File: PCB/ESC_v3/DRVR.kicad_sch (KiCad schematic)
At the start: 14 parts, among them U2 DRV8323SRTAT

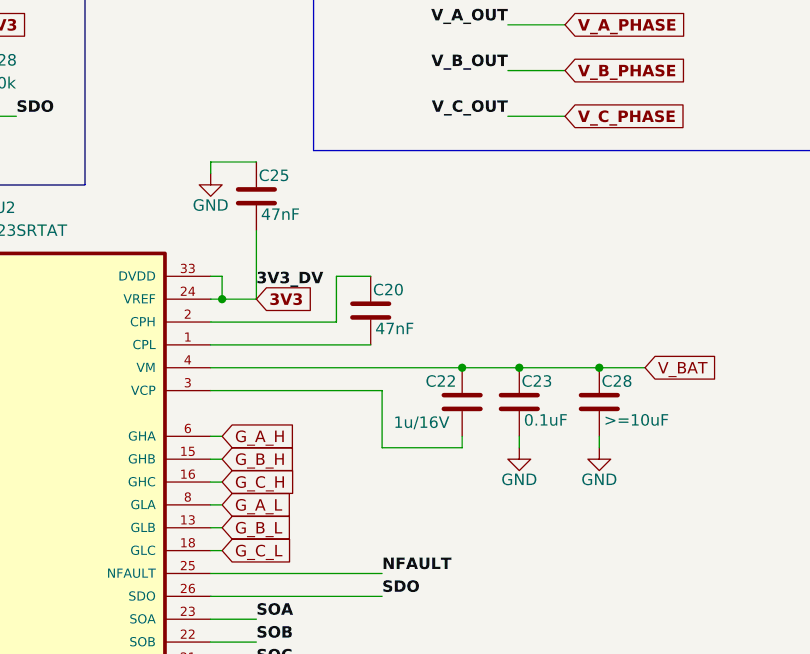
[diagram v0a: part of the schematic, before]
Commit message: Fix DRVR schematic wiring and PCB nets
Clean up DRVR.kicad_sch by adding/removing junctions and wires, rerouting traces and repositioning symbols; update component properties (capacitor values/ratings and label positions). Update ESC_v3.kicad_pcb to match schematic changes: reorder/renumber nets, correct pin/net assignments and adjust footprints/placements. Remove many outdated ESC_v3-backups ZIPs and add new timestamped backup ZIPs; add STM/STM.ioc and update MCU.kicad_sch and related project files. These changes correct net mappings and tidy schematic/PCB routing and metadata.
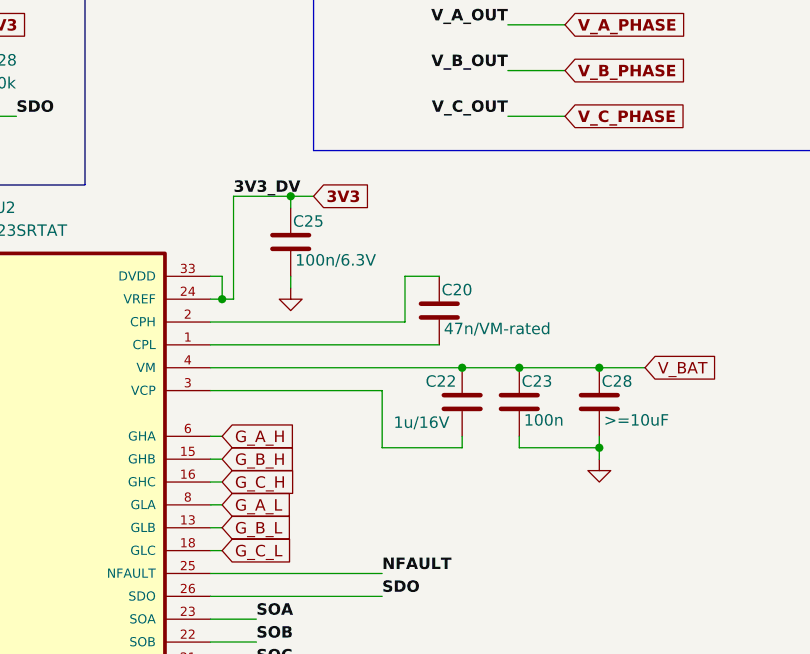
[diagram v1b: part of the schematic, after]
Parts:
- C20: value 47nF -> 47n/VM-rated
- C23: value 0.1uF -> 100n
- C25: value 47nF -> 100n/6.3V
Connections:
- net 3V3: now also C25.1; no longer C25.2
- net GND: now also C25.2; no longer C25.1
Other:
- moved on the sheet: C20, C25

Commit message: Updates
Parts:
- added C34: 100n/6.3V, Capacitor_SMD:C_0805_2012Metric, symbol Device:C
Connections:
- net EN_DV: now also C34.1
- net GND: now also C34.2
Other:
- moved on the sheet: R26
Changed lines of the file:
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@@
 	)
 	(junction
-		(at 40.64 41.91)
+		(at 41.91 35.56)
 		(diameter 0)
 		(color 0 0 0 0)
@@
 	(wire
 		(pts
-			(xy 40.64 41.91) (xy 45.72 41.91)
+			(xy 41.91 35.56) (xy 46.99 35.56)
 		)
 		(stroke
@@
 	(wire
 		(pts
-			(xy 40.64 41.91) (xy 40.64 40.64)
+			(xy 41.91 35.56) (xy 41.91 34.29)
 		)
 		(stroke
@@
 	(wire
 		(pts
+			(xy 41.91 35.56) (xy 41.91 36.83)
+		)
+		(stroke
+			(width 0)
+			(type default)
+		)
+	)
+	(wire
+		(pts
 			(xy 100.33 115.57) (xy 104.14 115.57)
 		)
@@
 	(wire
 		(pts
-			(xy 40.64 31.75) (xy 40.64 33.02)
+			(xy 41.91 25.4) (xy 41.91 26.67)
 		)
 		(stroke
@@
 	(wire
 		(pts
-			(xy 35.56 41.91) (xy 40.64 41.91)
+			(xy 36.83 35.56) (xy 41.91 35.56)
 		)
 		(stroke
@@
 	(wire
 		(pts
+			(xy 41.91 44.45) (xy 41.91 45.72)
+		)
+		(stroke
+			(width 0)
+			(type default)
+		)
+	)
+	(wire
+		(pts
 			(xy 30.48 69.85) (xy 30.48 73.66)
 		)
@@
 	)
 	(label "EN_DV"
-		(at 35.56 41.91 180)
+		(at 36.83 35.56 180)
 		(effects
 			(font
@@
 	)
 	(label "ENABLE"
-		(at 45.72 41.91 0)
+		(at 46.99 35.56 0)
 		(effects
 			(font
@@
 	(global_label "3V3"
 		(shape input)
-		(at 40.64 31.75 180)
+		(at 41.91 25.4 180)
 		(fields_autoplaced yes)
 		(effects
@@
 		)
 		(property "Intersheetrefs" "${INTERSHEET_REFS}"
-			(at 33.6712 31.75 0)
+			(at 34.9412 25.4 0)
 			(effects
 				(font
@@
 	(symbol
 		(lib_id "Device:C")
+		(at 41.91 40.64 0)
+		(unit 1)
+		(exclude_from_sim no)
+		(in_bom yes)
+		(on_board yes)
+		(dnp no)
+		(property "Reference" "C34"
+			(at 42.164 38.354 0)
+			(effects
+				(font
+					(size 1.27 1.27)
+				)
+				(justify left)
+			)
+		)
+		(property "Value" "100n/6.3V"
+			(at 42.418 42.672 0)
+			(effects
+				(font
+					(size 1.27 1.27)
+				)
+				(justify left)
+			)
+		)
+		(property "Footprint" "Capacitor_SMD:C_0805_2012Metric"
+			(at 42.8752 44.45 0)
+			(effects
+				(font
+					(size 1.27 1.27)
+				)
+				(hide yes)
+			)
+		)
+		(property "Datasheet" "~"
+			(at 41.91 40.64 0)
+			(effects
+				(font
+					(size 1.27 1.27)
+				)
+				(hide yes)
+			)
+		)
+		(property "Description" "Unpolarized capacitor"
+			(at 41.91 40.64 0)
+			(effects
+				(font
+					(size 1.27 1.27)
+				)
+				(hide yes)
+			)
+		)
+		(pin "1"
+		)
+		(pin "2"
+		)
+		(instances
+			(project "ESC_v3"
+				(path "/bb7f65bd-c3d2-4eba-8e72-fdc4c3d3399c/c36682af-7334-4ae4-b708-5014138612ef"
+					(reference "C34")
+					(unit 1)
+				)
+			)
+		)
+	)
+	(symbol
+		(lib_id "Device:C")
 		(at 184.15 73.66 0)
 		(unit 1)
@@
 	)
 	(symbol
+		(lib_id "power:GND")
+		(at 41.91 45.72 0)
+		(unit 1)
+		(exclude_from_sim no)
+		(in_bom yes)
+		(on_board yes)
+		(dnp no)
+		(property "Reference" "#PWR020"
+			(at 41.91 52.07 0)
+			(effects
+				(font
+					(size 1.27 1.27)
+				)
+				(hide yes)
+			)
+		)
+		(property "Value" "GND"
+			(at 41.91 49.276 0)
+			(effects
+				(font
+					(size 1.27 1.27)
+				)
+				(hide yes)
+			)
+		)
+		(property "Footprint" ""
+			(at 41.91 45.72 0)
+			(effects
+				(font
+					(size 1.27 1.27)
+				)
+				(hide yes)
+			)
+		)
+		(property "Datasheet" ""
+			(at 41.91 45.72 0)
+			(effects
+				(font
+					(size 1.27 1.27)
+				)
+				(hide yes)
+			)
+		)
+		(property "Description" "Power symbol creates a global label with name \"GND\" , ground"
+			(at 41.91 45.72 0)
+			(effects
+				(font
+					(size 1.27 1.27)
+				)
+				(hide yes)
+			)
+		)
+		(pin "1"
+		)
+		(instances
+			(project "ESC_v3"
+				(path "/bb7f65bd-c3d2-4eba-8e72-fdc4c3d3399c/c36682af-7334-4ae4-b708-5014138612ef"
+					(reference "#PWR020")
+					(unit 1)
+				)
+			)
+		)
+	)
+	(symbol
 		(lib_id "Device:R")
-		(at 40.64 36.83 180)
+		(at 41.91 30.48 180)
 		(unit 1)
 		(exclude_from_sim no)
@@
 		(dnp no)
 		(property "Reference" "R26"
-			(at 44.069 35.687 0)
+			(at 45.339 29.337 0)
 			(effects
 				(font
@@
 		)
 		(property "Value" "10k"
-			(at 44.069 38.227 0)
+			(at 45.339 31.877 0)
 			(effects
 				(font
@@
 		)
 		(property "Footprint" "Resistor_SMD:R_0603_1608Metric"
-			(at 42.418 36.83 90)
+			(at 43.688 30.48 90)
 			(effects
 				(font
@@
 		)
 		(property "Datasheet" "~"
-			(at 40.64 36.83 0)
+			(at 41.91 30.48 0)
 			(effects
 				(font
@@
 		)
 		(property "Description" "Resistor"
-			(at 40.64 36.83 0)
+			(at 41.91 30.48 0)
 			(effects
 				(font
@@
 					(size 1.27 1.27)
 				)
+				(hide yes)
 			)
 		)

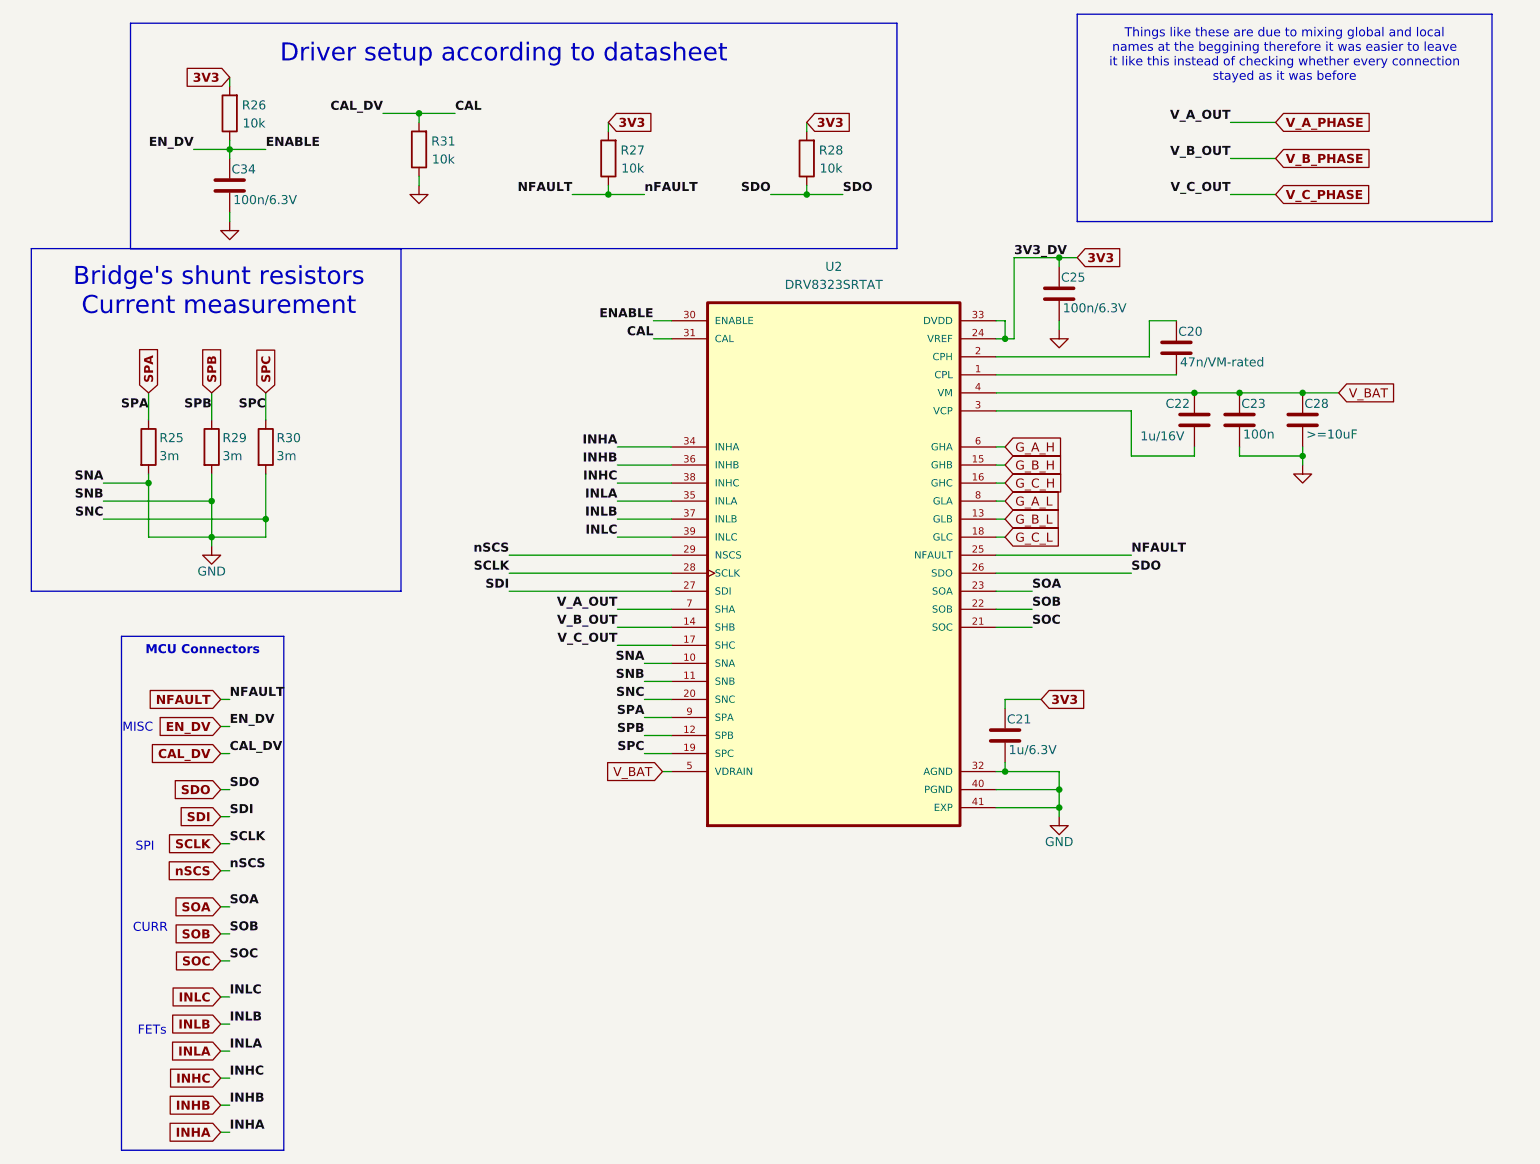
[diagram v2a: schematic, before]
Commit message: Update PCB layout and driver schematic
Adjust KiCad project files: many PCB footprint positions/rotations/uuids and silk/pad orientations updated, trace segments and widths adjusted, vias added/moved (several tented/free vias), and zone_connect enabled on referenced footprints. Correct MCU pin net assignments (PB4/PB5/PB6 / NFAULT / EN_DV) and other net fixes. In DRVR schematic change stroke styles to dashed and update a capacitor value from ">=10uF" to "22u". Remove several old backup zip files and add new backup snapshots. Miscellaneous small .kicad_prl/.kicad_sch/.ioc updates included for consistency and routing cleanup.
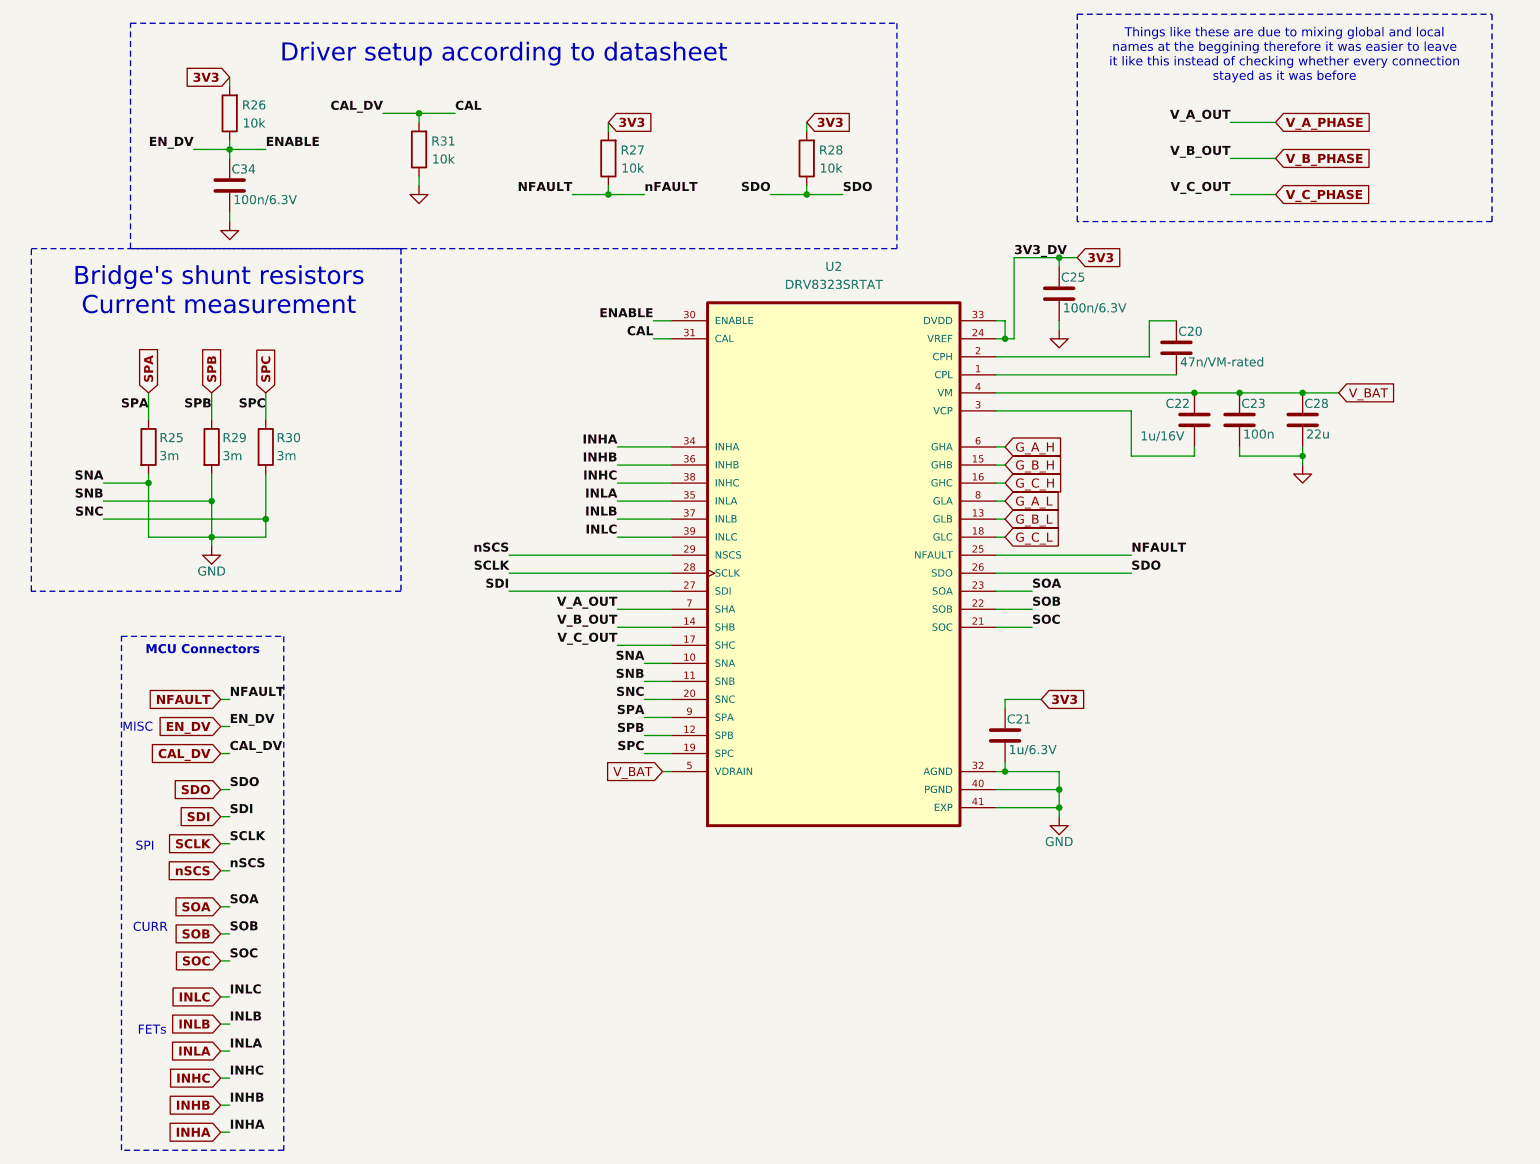
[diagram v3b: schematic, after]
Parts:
- C28: value >=10uF -> 22u
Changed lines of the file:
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@@
 		(stroke
 			(width 0)
-			(type default)
+			(type dash)
 		)
 		(fill
@@
 		(stroke
 			(width 0)
-			(type default)
+			(type dash)
 		)
 		(fill
@@
 		(stroke
 			(width 0)
-			(type default)
+			(type dash)
 		)
 		(fill
@@
 		(stroke
 			(width 0)
-			(type default)
+			(type dash)
 		)
 		(fill
@@
 			)
 		)
-		(property "Value" ">=10uF"
+		(property "Value" "22u"
 			(at 193.548 75.692 0)
 			(effects

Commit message: Reposition DRVR schematic elements
Adjust layout in PCB/ESC_v3/DRVR.kicad_sch: updated coordinates for rectangles, text labels, junctions, wires and pins to tidy and realign the driver schematic. Changes are graphical/coordinate-only (no netlist/electrical changes). Also touched project files (ESC_v3.*) and refreshed backup archives (deleted several older backups and added new snapshots).
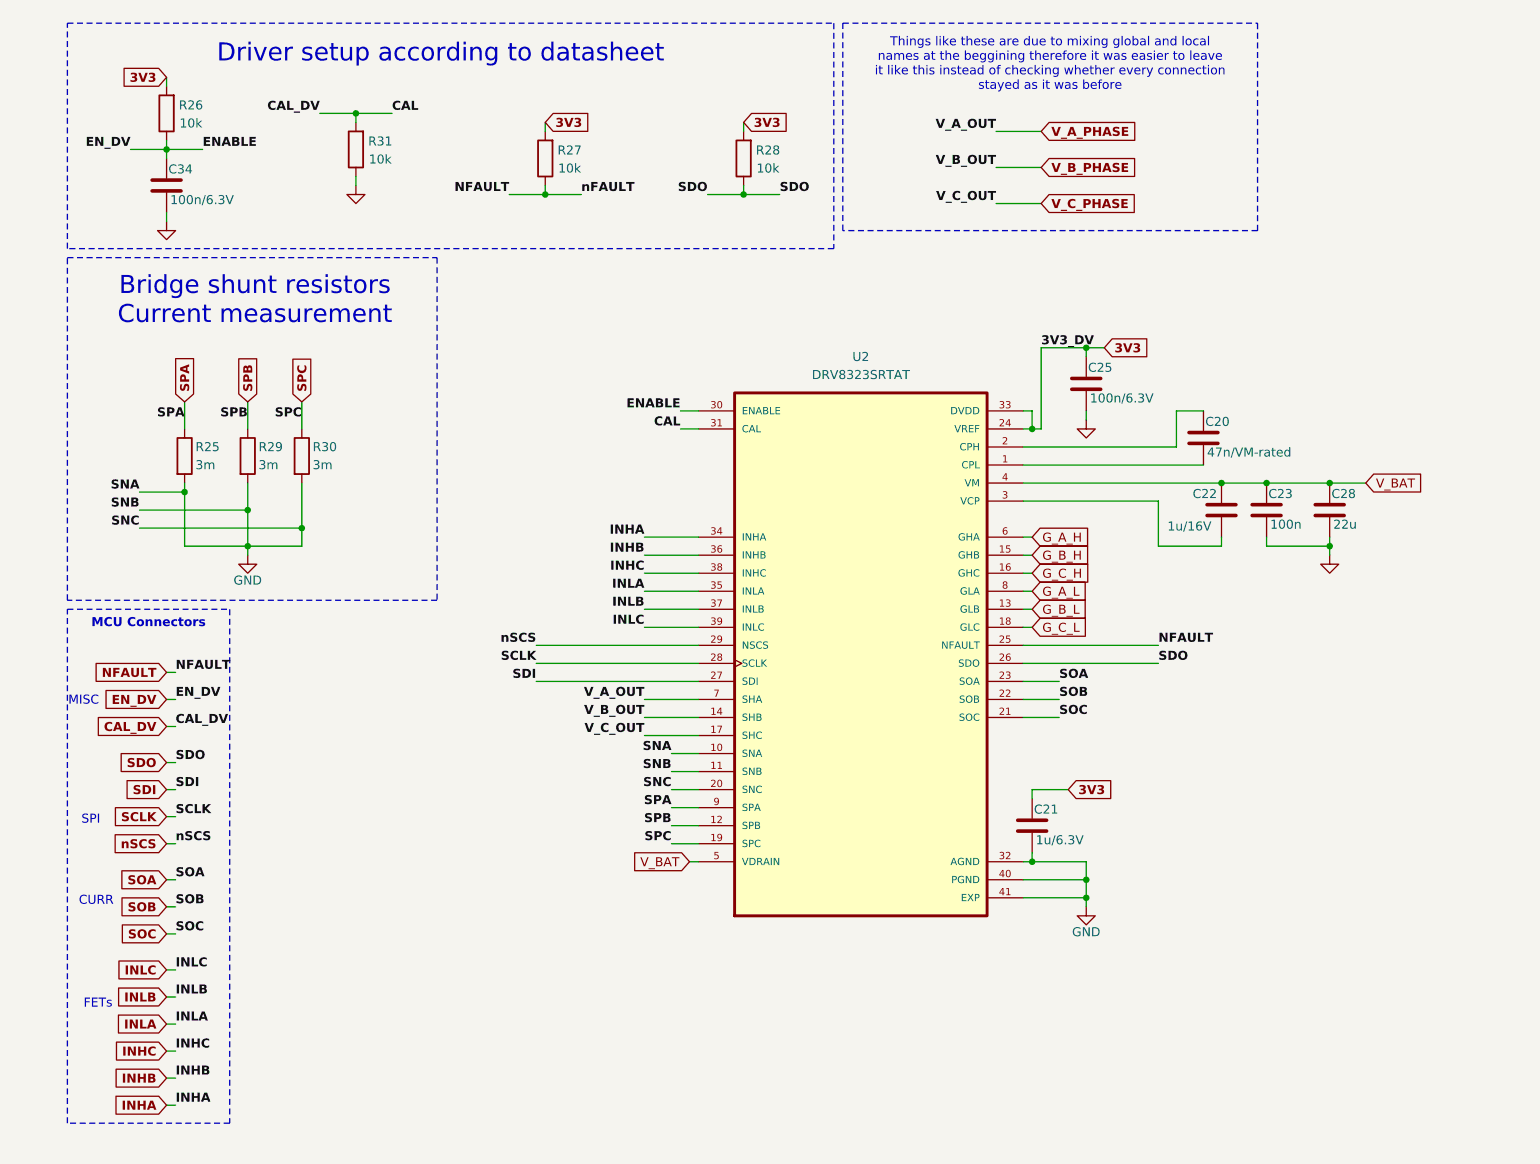
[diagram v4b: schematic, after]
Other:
- note added: "Bridge shunt resistors Current measurement"
- note removed: "Bridge's shunt resistors Current measurement"
- moved on the sheet: C20, C21, C22, C23, C25, C28, C34, R25, R26, R27, R28, R29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
